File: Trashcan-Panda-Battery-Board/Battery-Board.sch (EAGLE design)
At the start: 4 parts, among them J1 B2B-PH-SM4-TB(LF)(SN)

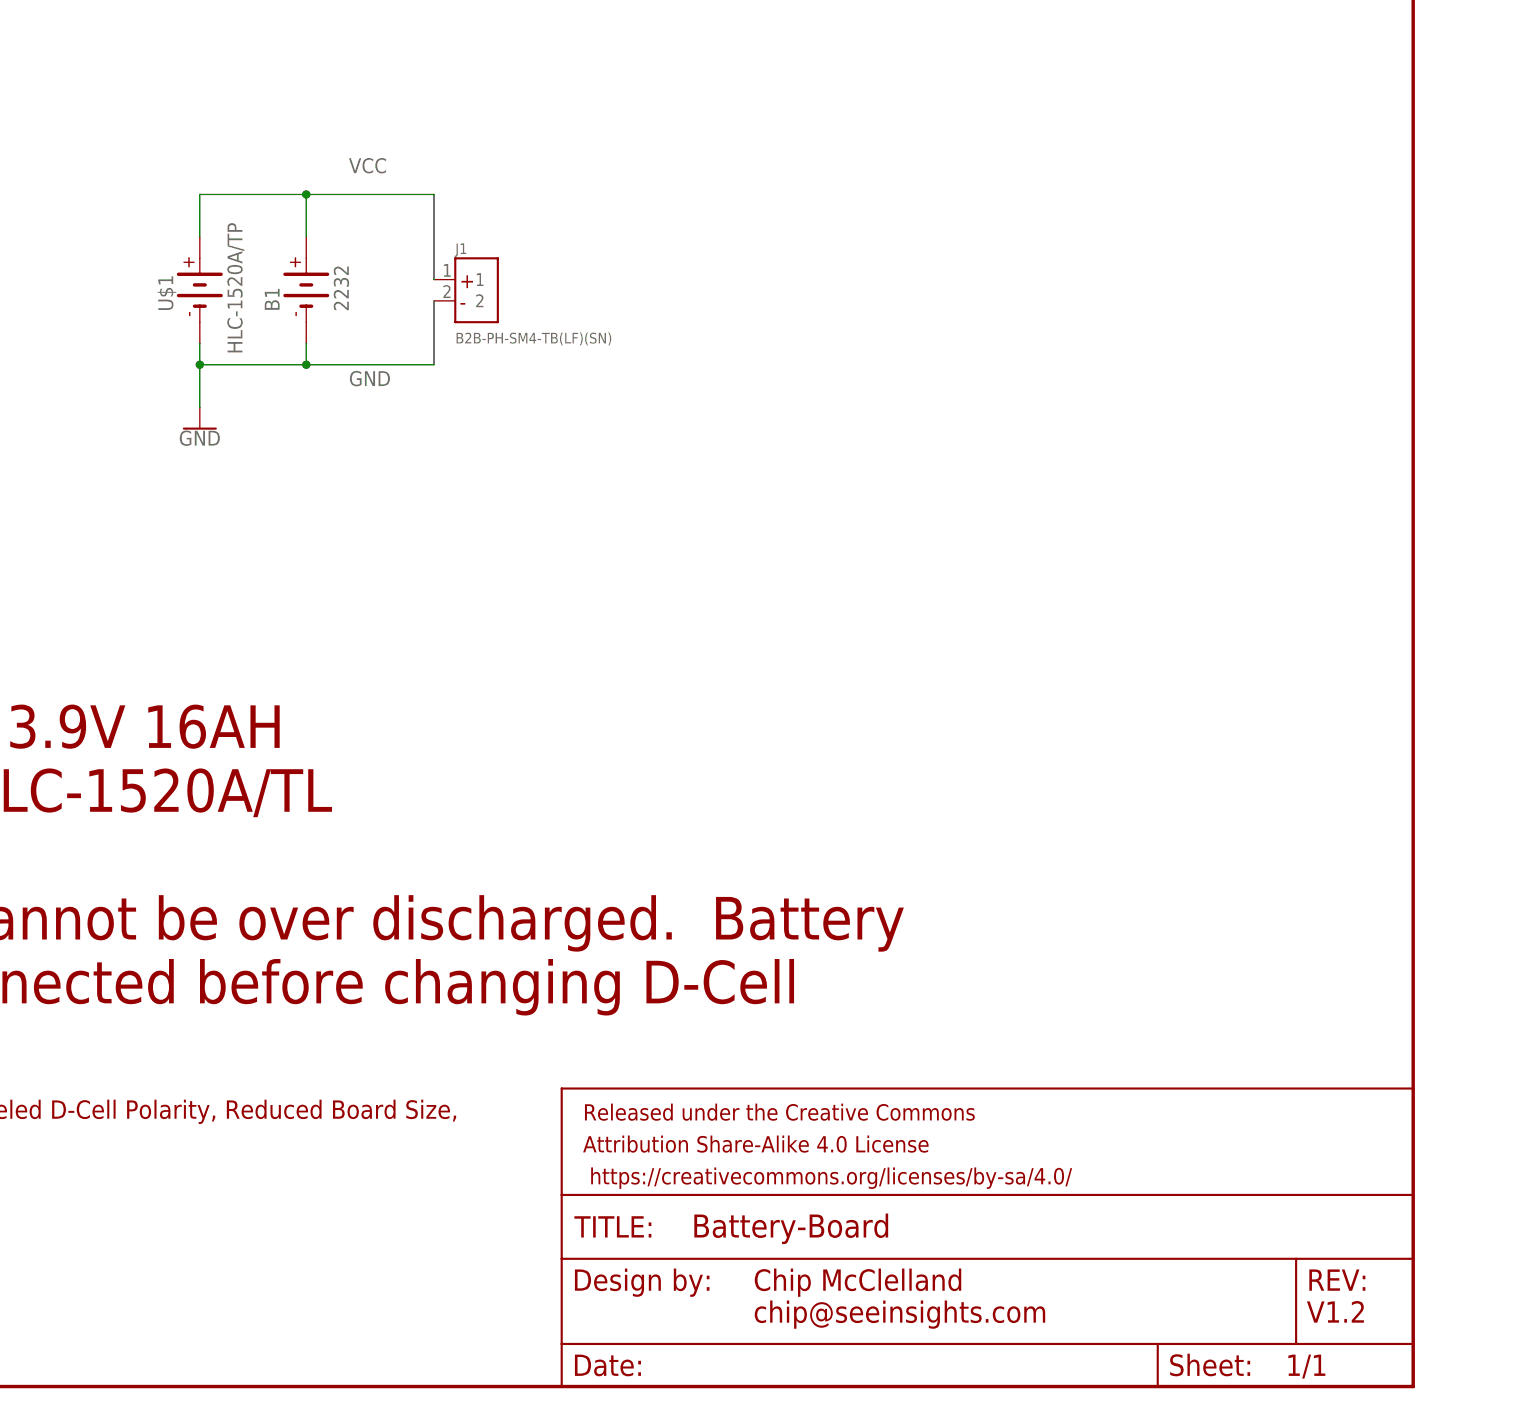
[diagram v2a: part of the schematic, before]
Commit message: Added PTC
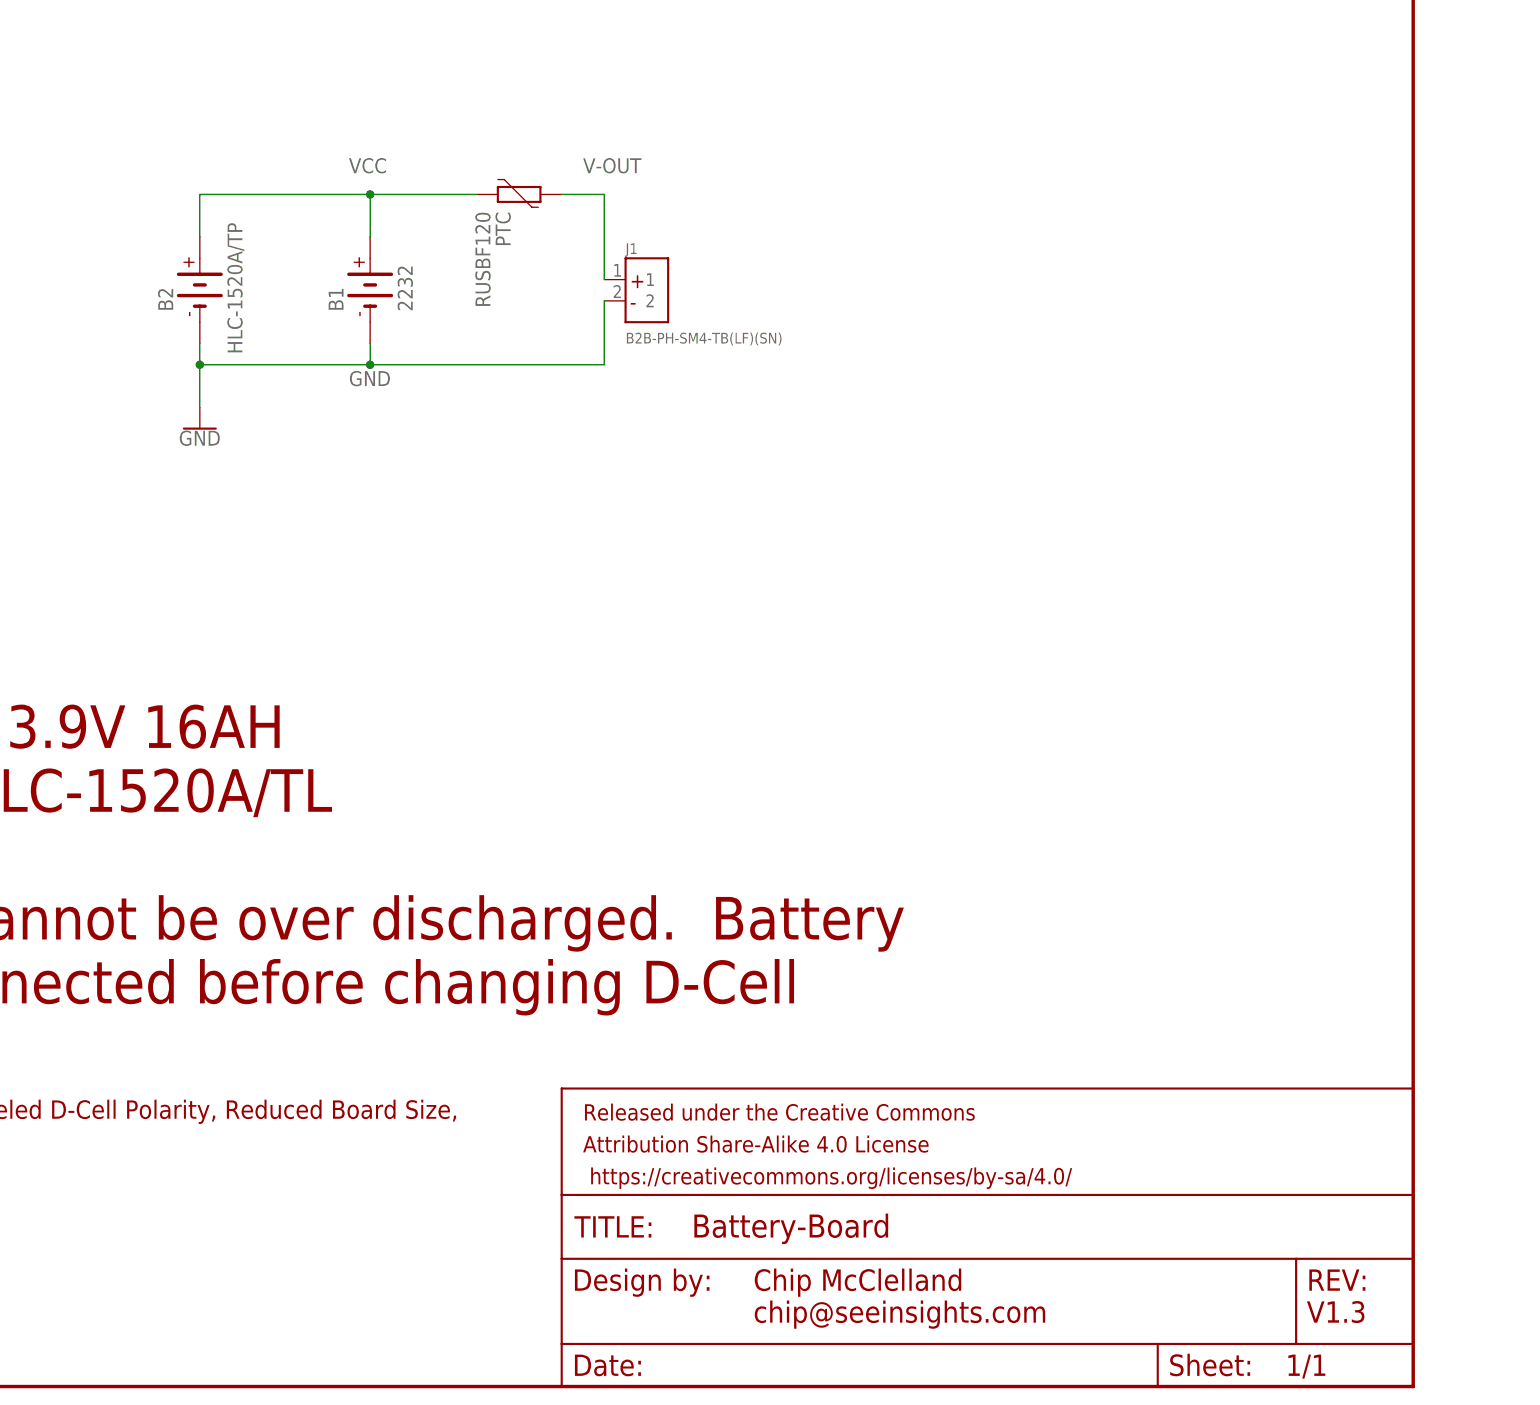
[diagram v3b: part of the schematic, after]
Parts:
- added PTC: RUSBF120, Battery-Board:RUSBF120
- renumbered U$1 to B2
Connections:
- new net V-OUT: J1.1, PTC.2
- net VCC: now also PTC.1; no longer J1.1
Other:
- note added: "V1.3"
- note removed: "V1.2"
- moved on the sheet: B1, J1
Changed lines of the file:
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@@
 <part name="B1" library="Battery-Board" deviceset="2232" device="" override_package3d_urn="urn:adsk.eagle:package:34202687/3" override_package_urn="urn:adsk.eagle:footprint:34202688/1" override_locally_modified="yes"/>
 <part name="J1" library="Custom Components" deviceset="B2B-PH-SM4-TB(LF)(SN)" device=""/>
-<part name="U$1" library="Battery-Board" deviceset="HLC-1520A/TP" device=""/>
+<part name="B2" library="Battery-Board" deviceset="HLC-1520A/TP" device=""/>
 <part name="FRAME1" library="SparkFun-Aesthetics" library_urn="urn:adsk.eagle:library:507" deviceset="FRAME-LETTER" device="" package3d_urn="urn:adsk.eagle:package:37121/1"/>
 <part name="GND1" library="SparkFun-PowerSymbols" library_urn="urn:adsk.eagle:library:530" deviceset="GND" device=""/>
+<part name="PTC" library="Battery-Board" deviceset="RUSBF120" device=""/>
 </parts>
 <sheets>
@@
 <text x="170.18" y="7.62" size="2.54" layer="94">Chip McClelland
 chip@seeinsights.com</text>
-<text x="236.22" y="7.62" size="2.54" layer="94">V1.2</text>
+<text x="236.22" y="7.62" size="2.54" layer="94">V1.3</text>
 <text x="17.78" y="25.4" size="2.1844" layer="94">Change Log
 V1.1  - Flipped the test point and labeled, Labeled D-Cell Polarity, Reduced Board Size,
@@
 </plain>
 <instances>
-<instance part="B1" gate="G$1" x="116.84" y="129.54" smashed="yes" rot="R90">
-<attribute name="NAME" x="113.661490625" y="128.2686" size="1.77996875" layer="95" rot="R90"/>
-<attribute name="VALUE" x="121.9233" y="128.26916875" size="1.779159375" layer="96" rot="R90"/>
+<instance part="B1" gate="G$1" x="124.46" y="129.54" smashed="yes" rot="R90">
+<attribute name="NAME" x="121.281490625" y="128.2686" size="1.77996875" layer="95" rot="R90"/>
+<attribute name="VALUE" x="129.5433" y="128.26916875" size="1.779159375" layer="96" rot="R90"/>
 </instance>
-<instance part="J1" gate="G$1" x="137.16" y="132.08" smashed="yes">
-<attribute name="NAME" x="134.61638125" y="135.132340625" size="1.271809375" layer="95"/>
-<attribute name="VALUE" x="134.61901875" y="124.457059375" size="1.270490625" layer="96"/>
+<instance part="J1" gate="G$1" x="157.48" y="132.08" smashed="yes">
+<attribute name="NAME" x="154.93638125" y="135.132340625" size="1.271809375" layer="95"/>
+<attribute name="VALUE" x="154.93901875" y="124.457059375" size="1.270490625" layer="96"/>
 </instance>
-<instance part="U$1" gate="G$1" x="104.14" y="129.54" smashed="yes" rot="R90">
+<instance part="B2" gate="G$1" x="104.14" y="129.54" smashed="yes" rot="R90">
 <attribute name="NAME" x="100.961490625" y="128.2686" size="1.77996875" layer="95" rot="R90"/>
 <attribute name="VALUE" x="109.2233" y="123.18916875" size="1.779159375" layer="96" rot="R90"/>
@@
 <attribute name="VALUE" x="104.14" y="114.046" size="1.778" layer="96" align="top-center"/>
 </instance>
+<instance part="PTC" gate="G$1" x="142.24" y="142.24" smashed="yes" rot="R270">
+<attribute name="NAME" x="139.446" y="140.1826" size="1.778" layer="95" rot="R270"/>
+<attribute name="VALUE" x="137.033" y="140.208" size="1.778" layer="96" rot="R270"/>
+</instance>
 </instances>
 <busses>
@@
 <segment>
 <pinref part="J1" gate="G$1" pin="2"/>
-<wire x1="104.14" y1="121.92" x2="116.84" y2="121.92" width="0.1524" layer="91"/>
-<wire x1="116.84" y1="121.92" x2="132.08" y2="121.92" width="0.1524" layer="91"/>
-<wire x1="132.08" y1="121.92" x2="132.08" y2="129.54" width="0.1524" layer="91"/>
-<pinref part="U$1" gate="G$1" pin="-"/>
+<wire x1="104.14" y1="121.92" x2="124.46" y2="121.92" width="0.1524" layer="91"/>
+<wire x1="124.46" y1="121.92" x2="152.4" y2="121.92" width="0.1524" layer="91"/>
+<wire x1="152.4" y1="121.92" x2="152.4" y2="129.54" width="0.1524" layer="91"/>
+<pinref part="B2" gate="G$1" pin="-"/>
 <wire x1="104.14" y1="124.46" x2="104.14" y2="121.92" width="0.1524" layer="91"/>
 <pinref part="B1" gate="G$1" pin="-"/>
-<wire x1="116.84" y1="124.46" x2="116.84" y2="121.92" width="0.1524" layer="91"/>
-<junction x="116.84" y="121.92"/>
+<wire x1="124.46" y1="124.46" x2="124.46" y2="121.92" width="0.1524" layer="91"/>
+<junction x="124.46" y="121.92"/>
 <label x="121.92" y="119.38" size="1.778" layer="95"/>
 <pinref part="GND1" gate="1" pin="GND"/>
@@
 <net name="VCC" class="0">
 <segment>
-<pinref part="J1" gate="G$1" pin="1"/>
-<wire x1="104.14" y1="142.24" x2="116.84" y2="142.24" width="0.1524" layer="91"/>
-<wire x1="116.84" y1="142.24" x2="132.08" y2="142.24" width="0.1524" layer="91"/>
-<wire x1="132.08" y1="142.24" x2="132.08" y2="132.08" width="0.1524" layer="91"/>
-<pinref part="U$1" gate="G$1" pin="+"/>
+<wire x1="104.14" y1="142.24" x2="124.46" y2="142.24" width="0.1524" layer="91"/>
+<wire x1="124.46" y1="142.24" x2="137.16" y2="142.24" width="0.1524" layer="91"/>
+<pinref part="B2" gate="G$1" pin="+"/>
 <wire x1="104.14" y1="137.16" x2="104.14" y2="142.24" width="0.1524" layer="91"/>
 <pinref part="B1" gate="G$1" pin="+"/>
-<wire x1="116.84" y1="137.16" x2="116.84" y2="142.24" width="0.1524" layer="91"/>
-<junction x="116.84" y="142.24"/>
+<wire x1="124.46" y1="137.16" x2="124.46" y2="142.24" width="0.1524" layer="91"/>
+<junction x="124.46" y="142.24"/>
 <label x="121.92" y="144.78" size="1.778" layer="95"/>
+<pinref part="PTC" gate="G$1" pin="1"/>
 </segment>
 </net>
+<net name="V-OUT" class="0">
+<segment>
+<pinref part="PTC" gate="G$1" pin="2"/>
+<pinref part="J1" gate="G$1" pin="1"/>
+<wire x1="147.32" y1="142.24" x2="152.4" y2="142.24" width="0.1524" layer="91"/>
+<wire x1="152.4" y1="142.24" x2="152.4" y2="132.08" width="0.1524" layer="91"/>
+<label x="149.86" y="144.78" size="1.778" layer="95"/>
+</segment>
+</net>
